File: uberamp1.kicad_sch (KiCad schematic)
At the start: 8 parts

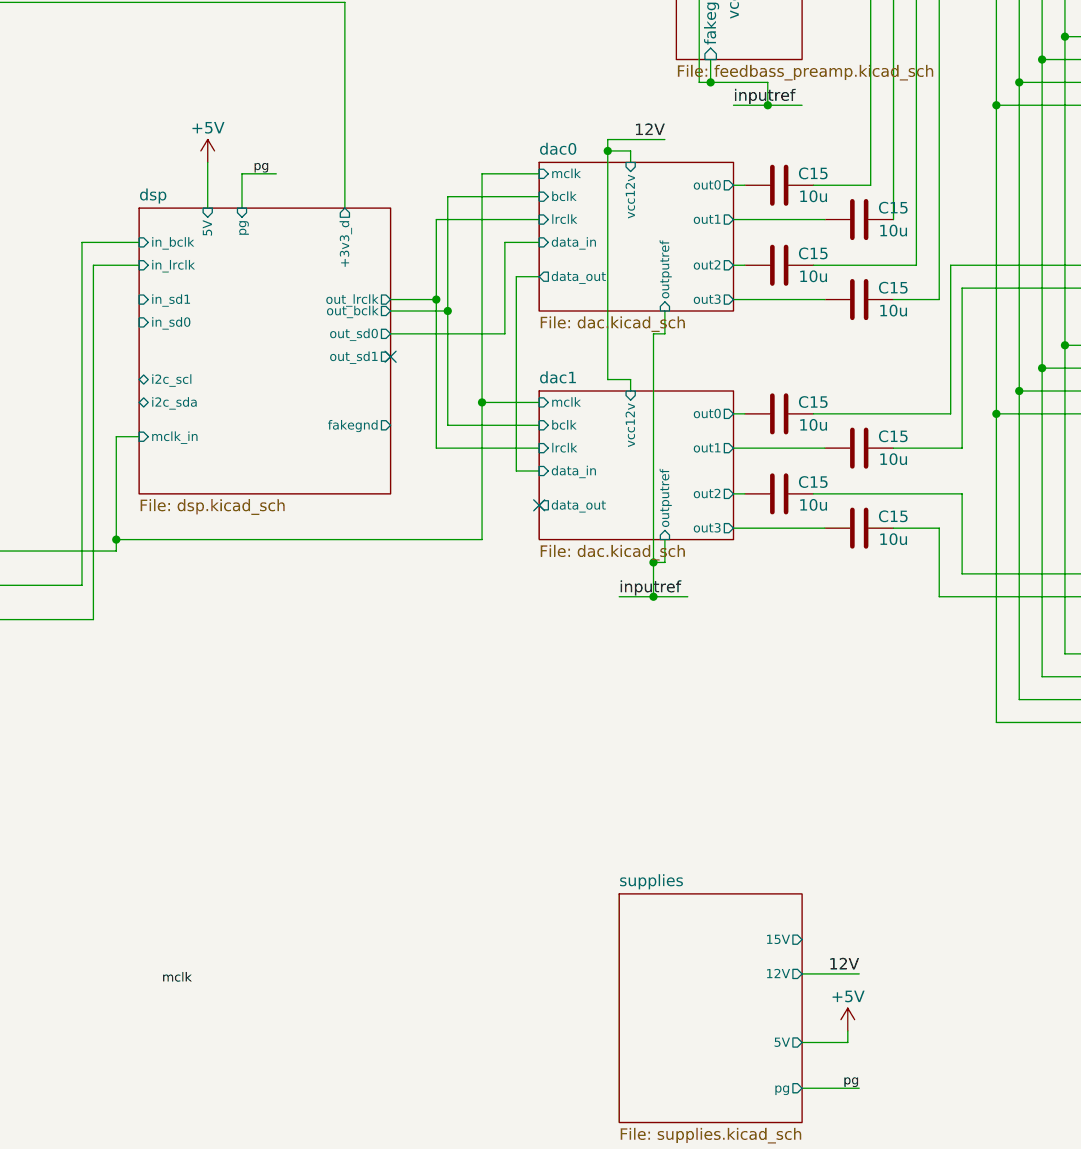
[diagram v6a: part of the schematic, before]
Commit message: update to kicad 8
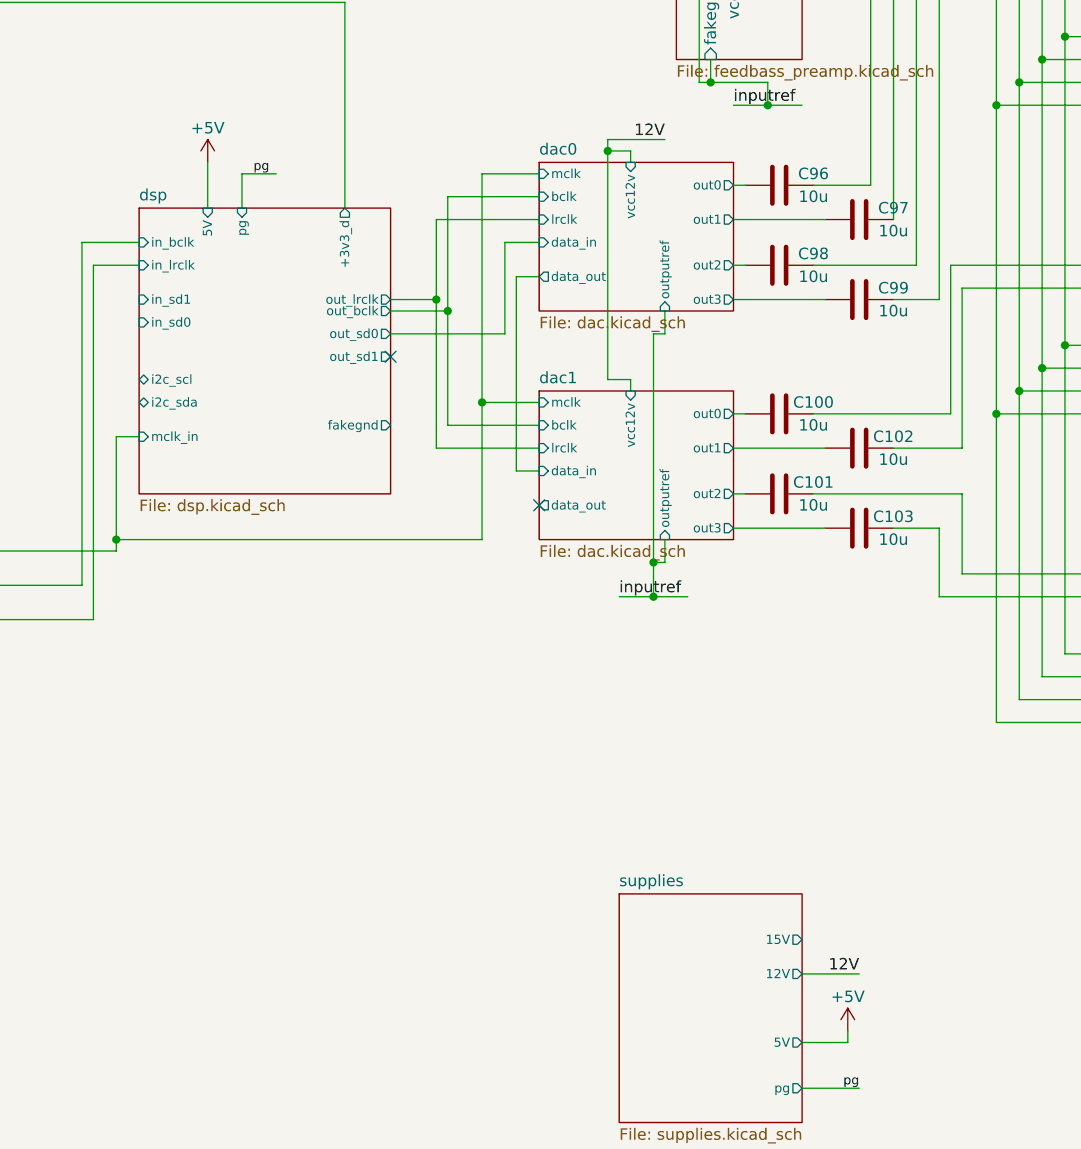
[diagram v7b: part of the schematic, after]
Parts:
- renumbered C15 to C100, C15 to C101, C15 to C102, C15 to C103, C15 to C96, C15 to C97, C15 to C98, C15 to C99

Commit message: schematic: some fixes
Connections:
- no-connect marks 3 -> 6
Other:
- sheet dac0 ports: added 3V3; removed none
- sheet dac1 ports: added 3V3; removed none
- sheet esp32 ports: added 5V, i2c_scl, i2c_sda, i2s_bclk_in, i2s_lrclk_in, i2s_sd_out, pg; removed none
